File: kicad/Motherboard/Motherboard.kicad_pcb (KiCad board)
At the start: 2 copper layers, 56 parts, among them J1 USB_C_Receptacle_USB2.0, J2 Conn_01x16_Pin, J3 Conn_01x16_Pin, J4 Conn_01x16_Pin, J5 Conn_01x02_Pin, J6 Conn_01x04_Pin, J7 Conn_01x04_Pin, J8 Conn_01x16_Pin, Q1 DMN3404L, SW1 Reset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

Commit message: This commit actually has the changes
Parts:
- moved C3 46.2 mm to (179.4, 127.0)
- moved C13 45.7 mm to (162.2, 132.8)
- moved C15 45.7 mm to (222.3, 91.2)
- moved C2 45.7 mm to (222.3, 88.7)
- moved C8 45.7 mm to (137.3, 140.9)
- moved C9 45.7 mm to (162.2, 121.4)
- moved D1 45.7 mm to (145.3, 160.3)
- moved J5 45.7 mm to (150.4, 146.8)
- moved L1 45.7 mm to (156.9, 150.9)
- moved U9 45.7 mm to (135.4, 177.2)
- moved C10 45.7 mm to (162.2, 125.5)
- moved C11 45.7 mm to (162.2, 128.9)
- moved C16 45.7 mm to (193.8, 96.3)
- moved C17 45.7 mm to (193.8, 98.1)
- moved C19 45.7 mm to (222.3, 93.7)
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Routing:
- net bit3: track 0.00 -> 118.3 mm, vias 0 -> 8
- net EN2: track 0.00 -> 95.4 mm, vias 0 -> 2
- net COM2: track 0.00 -> 82.3 mm, vias 0 -> 2
- net +5V: track 0.00 -> 79.7 mm
- net bit0: track 0.00 -> 79.0 mm, vias 0 -> 4
- net bit2: track 0.00 -> 77.9 mm, vias 0 -> 4
- net EN3: track 0.00 -> 69.6 mm, vias 0 -> 2
- net COM3: track 0.00 -> 55.8 mm, vias 0 -> 2
- net EN1: track 0.00 -> 51.2 mm, vias 0 -> 2
- net COM1: track 0.00 -> 41.4 mm
- net EN0: track 0.00 -> 35.6 mm, vias 0 -> 2
- net Net-(J3-Pin_8): track 0.00 -> 23.6 mm
- net Net-(J3-Pin_9): track 0.00 -> 23.5 mm
- net Net-(J8-Pin_8): track 0.00 -> 23.3 mm
- net Net-(J4-Pin_8): track 0.00 -> 23.3 mm
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
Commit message: Didnt save yet
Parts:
- moved U7 50.8 mm to (151.0, 80.9), turned to 90 degrees
- moved J2 49.4 mm to (94.1, 68.4)
- moved U5 49.4 mm to (109.3, 136.8)
- moved U6 49.4 mm to (109.3, 110.4)
- moved SW1 49.4 mm to (119.0, 49.9)
- moved U1 49.4 mm to (143.1, 50.4)
- moved U3 49.4 mm to (109.3, 59.1)
- moved U4 49.4 mm to (109.3, 85.5)
- moved J3 49.4 mm to (94.0, 146.8)
- moved J4 49.4 mm to (94.0, 119.9)
- moved J8 49.4 mm to (94.0, 95.0)
- moved SW2 49.4 mm to (146.6, 72.1)
- moved U8 43.1 mm to (134.2, 80.4), turned to 0 degrees
- moved C12 26.3 mm to (184.0, 89.5)
- moved C13 26.3 mm to (160.8, 106.6)
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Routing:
- net bit2: track 77.9 -> 114.0 mm, vias 4 -> 8
- net GND: track 16.3 -> 0.20 mm

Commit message: idk what the fuck this is
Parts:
- moved J4 101.5 mm to (188.1, 82.0), turned to 0 degrees
- moved C2 97.4 mm to (142.1, 119.8), turned to -90 degrees
- moved J8 94.5 mm to (188.1, 103.5), turned to 0 degrees
- moved C15 94.0 mm to (142.1, 116.4), turned to 90 degrees
- moved U4 71.6 mm to (177.1, 108.5), turned to 90 degrees
- moved SW1 71.3 mm to (161.0, 107.5), turned to 180 degrees
- moved U6 69.2 mm to (177.0, 96.0), turned to 90 degrees
- moved C17 65.9 mm to (143.5, 116.0), turned to 90 degrees
- moved C19 64.5 mm to (179.0, 116.5), turned to -90 degrees
- moved C24 61.5 mm to (163.0, 112.5), turned to 0 degrees
- moved C22 57.5 mm to (163.0, 114.5), turned to 0 degrees
- moved C23 56.5 mm to (163.0, 110.5), turned to 0 degrees
- moved J1 56.3 mm to (155.5, 107.5), turned to 180 degrees
- moved C21 52.5 mm to (167.0, 112.5)
- moved J2 51.3 mm to (133.5, 101.2)
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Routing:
- net GND: track 0.20 -> 283.0 mm, vias 0 -> 11
- net +3.3V: track 0.00 -> 119.4 mm, vias 0 -> 6
- net UART_1: track 0.00 -> 118.5 mm, vias 0 -> 6
- net bit1: track 0.00 -> 106.5 mm, vias 0 -> 7
- net VS_1: track 0.00 -> 99.4 mm, vias 0 -> 7
- net COM2: track 82.3 -> 6.18 mm, vias 2 -> 0
- net VCP_1: track 0.00 -> 71.9 mm, vias 0 -> 4
- net EN2: track 95.4 -> 29.0 mm
- net ENN_2: track 0.00 -> 51.4 mm, vias 0 -> 4
- net MAGCT: track 0.00 -> 46.9 mm, vias 0 -> 4
- net Net-(U1-EN): track 18.5 -> 60.5 mm, vias 0 -> 5
- net COM3: track 55.8 -> 13.9 mm
- net +5V: track 79.7 -> 119.3 mm, vias 0 -> 4
- net Net-(D2-A): track 0.00 -> 36.3 mm
- net DIR_2: track 0.00 -> 36.1 mm, vias 0 -> 2
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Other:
- board outline added: 77 x 63 mm
- board text removed: "${REFERENCE}"

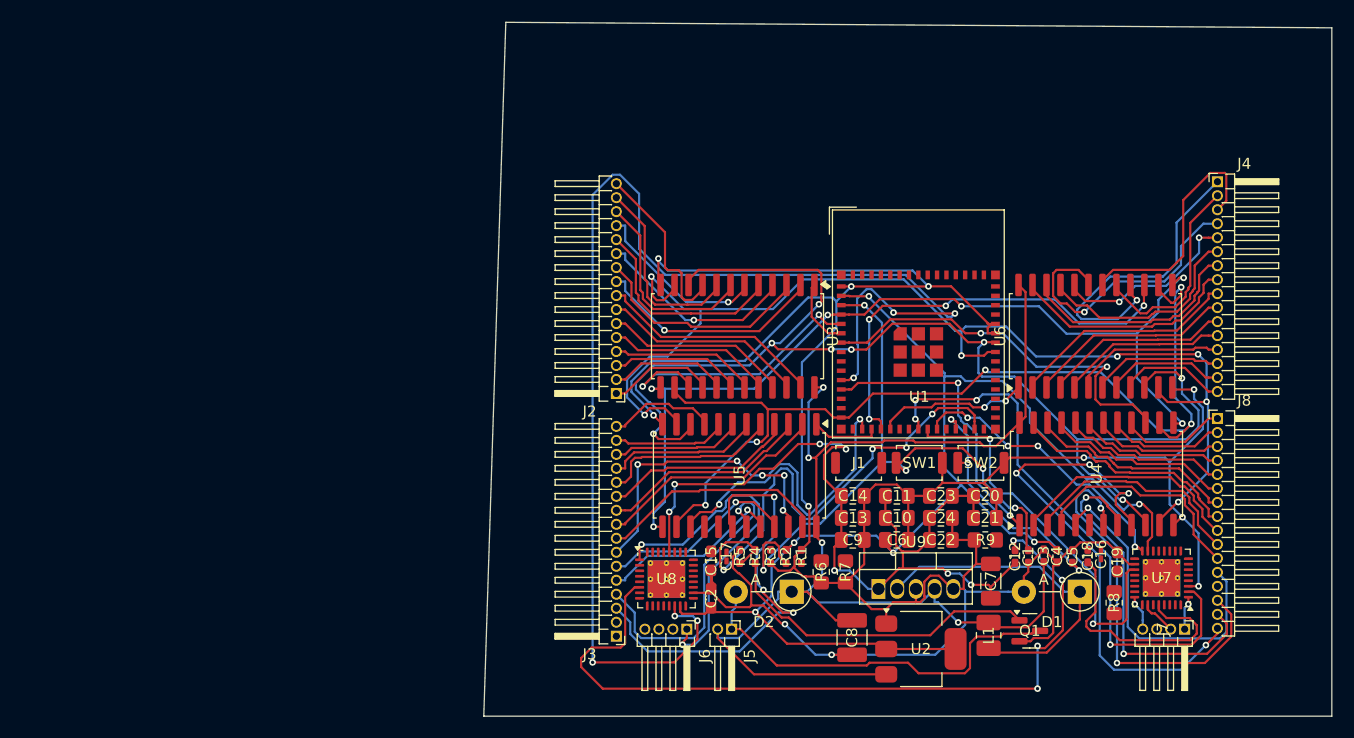
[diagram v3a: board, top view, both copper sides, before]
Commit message: updated layout
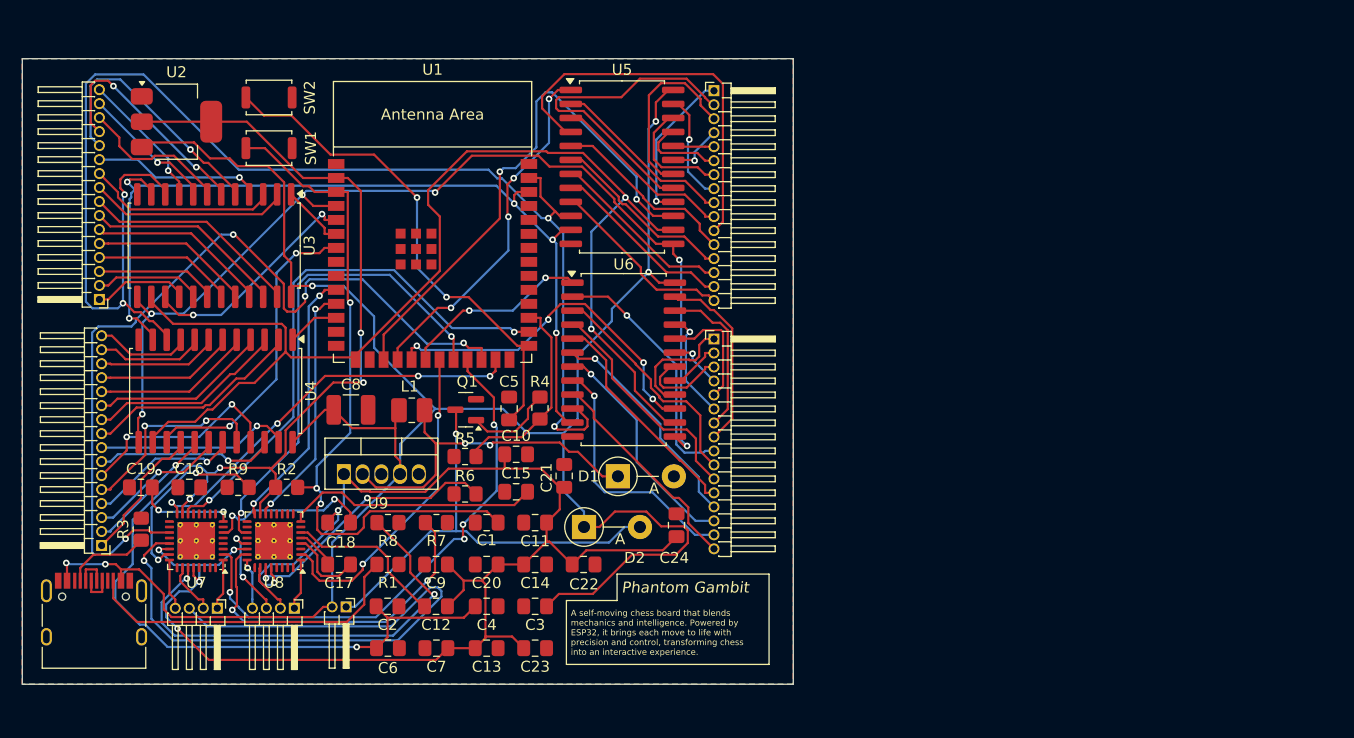
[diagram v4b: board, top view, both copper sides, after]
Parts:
- C1, C12, C18, C3, C4, C5: footprint Capacitor_SMD:C_0402_1005Metric_Pad0.74x0.62mm_HandSolder -> Capacitor_SMD:C_0805_2012Metric_Pad1.18x1.45mm_HandSolder
- C15, C19, C2: footprint Capacitor_SMD:C_0603_1608Metric_Pad1.08x0.95mm_HandSolder -> Capacitor_SMD:C_0805_2012Metric_Pad1.18x1.45mm_HandSolder
- C16, C17: footprint Capacitor_SMD:C_0201_0603Metric_Pad0.64x0.40mm_HandSolder -> Capacitor_SMD:C_0805_2012Metric_Pad1.18x1.45mm_HandSolder
- C7: footprint Capacitor_SMD:C_1206_3216Metric_Pad1.33x1.80mm_HandSolder -> Capacitor_SMD:C_0805_2012Metric_Pad1.18x1.45mm_HandSolder
- J1: footprint Button_Switch_SMD:SW_Push_SPST_NO_Alps_SKRK -> Connector_USB:USB_C_Receptacle_HRO_TYPE-C-31-M-12
- R1, R2, R3, R4, R5: footprint Resistor_SMD:R_0402_1005Metric_Pad0.72x0.64mm_HandSolder -> Resistor_SMD:R_0805_2012Metric_Pad1.20x1.40mm_HandSolder
- U1: footprint RF_Module:ESP32-S2-MINI-1 -> Espressif:ESP32-S2-SOLO
- moved J8 102.0 mm to (86.8, 115.0), turned to 180 degrees
- moved C19 88.9 mm to (90.4, 109.7), turned to 0 degrees
- moved J7 87.9 mm to (97.3, 120.7)
- moved U7 87.7 mm to (95.4, 114.6)
- moved C16 83.0 mm to (94.8, 109.7), turned to 0 degrees
- moved U2 82.8 mm to (93.6, 76.5)
- moved U4 80.3 mm to (97.2, 101.0), turned to -90 degrees
- moved SW2 72.7 mm to (102.0, 74.3)
- moved J1 71.0 mm to (86.1, 122.2), turned to 0 degrees
- moved C18 68.0 mm to (108.4, 112.9), turned to 0 degrees
- moved R9 68.0 mm to (99.2, 109.7)
- moved R8 66.3 mm to (112.8, 112.9), turned to 180 degrees
- moved SW1 65.6 mm to (102.0, 78.9)
- moved R3 57.2 mm to (90.4, 113.5), turned to 90 degrees
- moved L1 56.2 mm to (115.0, 102.7), turned to 180 degrees
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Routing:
- net GND: track 283.0 -> 0.00 mm, vias 11 -> 0
- net UART_1: track 118.5 -> 22.6 mm, vias 6 -> 2
- net +5V: track 119.3 -> 201.1 mm, vias 4 -> 5
- net Motor2_2: track 0.00 -> 63.3 mm, vias 0 -> 1
- net VCP_1: track 71.9 -> 14.7 mm, vias 4 -> 0
- net UART_2: track 0.00 -> 49.9 mm, vias 0 -> 2
- net DIR_1: track 0.00 -> 44.1 mm, vias 0 -> 2
- net Net-(U7-BRB): track 0.00 -> 41.7 mm, vias 0 -> 2
- net DIR_2: track 36.1 -> 77.3 mm, vias 2 -> 4
- net Net-(J8-Pin_16): track 48.9 -> 8.71 mm, vias 4 -> 0
- net VS_1: track 99.4 -> 134.2 mm, vias 7 -> 6
- net Net-(U8-BRA): track 0.00 -> 31.6 mm, vias 0 -> 2
- net Net-(J3-Pin_2): track 0.00 -> 30.5 mm
- net Net-(J1-CC2): track 0.00 -> 30.0 mm
- net ENN_1: track 0.00 -> 29.7 mm, vias 0 -> 2
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- added copper zone on B.Cu, net GND
- added copper zone on F.Cu, net GND
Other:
- board size 77 x 63 mm -> 70 x 56.8 mm
- board text added: "A self-moving chess board that blends mechanics and intelligence. Powered by ESP32, it brings each move to life with precision and control, transforming chess into an interactive experience."
- board text added: "Phantom Gambit"

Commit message: updated schematic
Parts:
- moved R3 84.6 mm to (172.2, 91.9), turned to 0 degrees
- moved J1 77.2 mm to (163.2, 118.0)
- moved R9 73.0 mm to (172.2, 109.6)
- moved R2 71.7 mm to (172.2, 89.0)
- moved R1 66.9 mm to (172.2, 86.0), turned to 0 degrees
- moved U2 66.0 mm to (142.9, 120.4)
- moved J8 62.8 mm to (142.6, 86.2), turned to 0 degrees
- moved SW2 62.6 mm to (134.0, 128.1)
- moved R8 59.8 mm to (172.2, 106.7), turned to 0 degrees
- moved L1 57.8 mm to (171.7, 114.1), turned to 0 degrees
- moved Q1 56.2 mm to (171.3, 125.1), turned to 0 degrees
- moved R7 55.8 mm to (172.2, 103.7), turned to 0 degrees
- moved SW1 55.0 mm to (134.0, 123.7), turned to 0 degrees
- moved U9 54.0 mm to (159.7, 126.6)
- moved J7 53.5 mm to (150.8, 121.1), turned to 0 degrees
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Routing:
- net +5V: track 201.1 -> 0.00 mm, vias 5 -> 0
- net VS_1: track 134.2 -> 0.00 mm, vias 6 -> 0
- net bit0: track 126.2 -> 0.00 mm, vias 4 -> 0
- net +3.3V: track 124.0 -> 0.00 mm, vias 5 -> 0
- net bit2: track 109.1 -> 0.00 mm, vias 2 -> 0
- net bit3: track 95.1 -> 0.00 mm, vias 6 -> 0
- net bit1: track 81.1 -> 0.00 mm, vias 5 -> 0
- net DIR_2: track 77.3 -> 0.00 mm, vias 4 -> 0
- net Net-(U1-EN): track 63.4 -> 0.00 mm, vias 3 -> 0
- net Motor2_2: track 63.3 -> 0.00 mm, vias 1 -> 0
- net UART_2: track 49.9 -> 0.00 mm, vias 2 -> 0
- net EN2: track 48.4 -> 0.00 mm, vias 2 -> 0
- net ENN_2: track 48.3 -> 0.00 mm, vias 4 -> 0
- net Net-(U1-GPIO0): track 46.0 -> 0.00 mm, vias 2 -> 0
- net DIR_1: track 44.1 -> 0.00 mm, vias 2 -> 0
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- removed copper zone on B.Cu, net GND
- removed copper zone on F.Cu, net GND
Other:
- board outline removed
- board text removed: "A self-moving chess board that blends mechanics and intelligence. Powered by ESP32, it brings each move to life with precision and control, transforming chess into an interactive experience."
- board text removed: "Phantom Gambit"

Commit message: added stuff
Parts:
- added J9: Conn_01x02_Pin, Connector_PinHeader_1.27mm:PinHeader_1x02_P1.27mm_Vertical, F.Cu at (129.6, 106.5)
- J2, J3, J4, J8: footprint Connector_PinHeader_1.27mm:PinHeader_1x16_P1.27mm_Horizontal -> Connector_PinHeader_1.27mm:PinHeader_1x16_P1.27mm_Vertical
- J5: footprint Connector_PinHeader_1.27mm:PinHeader_1x02_P1.27mm_Horizontal -> Connector_PinHeader_1.27mm:PinHeader_1x02_P1.27mm_Vertical
- J6, J7: footprint Connector_PinHeader_1.27mm:PinHeader_1x04_P1.27mm_Horizontal -> Connector_PinHeader_1.27mm:PinHeader_1x04_P1.27mm_Vertical
- moved C8 69.2 mm to (171.5, 62.2)
- moved Q1 54.6 mm to (170.9, 70.5)
- moved L1 47.9 mm to (171.1, 66.2)
- moved J2 41.5 mm to (158.8, 78.8)
- moved C1 39.5 mm to (144.7, 78.7)
- moved C10 39.5 mm to (149.5, 78.7)
- moved C11 39.5 mm to (149.5, 81.7)
- moved C12 39.5 mm to (149.5, 84.7)
- moved C13 39.5 mm to (149.5, 87.7)
- moved C14 39.5 mm to (149.5, 90.7)
- moved C15 39.5 mm to (149.5, 93.7)
- moved C16 39.5 mm to (149.5, 96.7)
- moved C17 39.5 mm to (149.5, 99.7)
- moved C18 39.5 mm to (154.4, 78.7)
- moved C19 39.5 mm to (154.4, 81.7)
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
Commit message: bet
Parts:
- J2, J3, J4, J8: footprint Connector_PinHeader_1.27mm:PinHeader_1x16_P1.27mm_Vertical -> Connector_PinHeader_2.54mm:PinHeader_1x16_P2.54mm_Vertical
- J5, J9: footprint Connector_PinHeader_1.27mm:PinHeader_1x02_P1.27mm_Vertical -> Connector_PinHeader_2.54mm:PinHeader_1x02_P2.54mm_Vertical
- J6, J7: footprint Connector_PinHeader_1.27mm:PinHeader_1x04_P1.27mm_Vertical -> Connector_PinHeader_2.54mm:PinHeader_1x04_P2.54mm_Vertical
- moved SW1 72.7 mm to (171.2, 55.4)
- moved SW2 72.7 mm to (171.2, 59.9)
- moved Q1 49.5 mm to (149.0, 114.9)
- moved J2 40.7 mm to (118.6, 72.6)
- moved J3 40.2 mm to (123.3, 72.6)
- moved J4 39.7 mm to (127.9, 72.6)
- moved J8 39.2 mm to (132.6, 72.6)
- moved R1 33.2 mm to (172.4, 71.7)
- moved R2 33.2 mm to (172.4, 74.7)
- moved R3 33.2 mm to (172.4, 77.6)
- moved R4 33.2 mm to (172.4, 80.6)
- moved R5 33.2 mm to (172.4, 83.5)
- moved R6 33.2 mm to (172.4, 86.5)
- moved R7 33.2 mm to (172.4, 89.4)
- moved R8 33.2 mm to (172.4, 92.4)
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
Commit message: TMC in
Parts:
- moved U6 148.8 mm to (67.0, 176.8), turned to 180 degrees
- moved J4 141.5 mm to (47.0, 188.7), turned to 90 degrees
- moved U3 124.3 mm to (35.0, 149.8), turned to 90 degrees
- moved U5 121.5 mm to (111.2, 177.4), turned to 180 degrees
- moved J3 120.5 mm to (91.6, 188.8), turned to 90 degrees
- moved J2 112.2 mm to (22.6, 130.7)
- moved J8 110.6 mm to (22.8, 85.4)
- moved U4 109.6 mm to (35.5, 106.2), turned to 90 degrees
- moved J6 109.3 mm to (51.2, 69.6)
- moved J7 109.3 mm to (55.9, 69.6)
- moved Q1 109.3 mm to (44.1, 84.2)
- moved U2 109.3 mm to (63.1, 80.8)
- moved C8 109.3 mm to (66.0, 33.6)
- moved R1 109.3 mm to (67.5, 41.1)
- moved R2 109.3 mm to (67.5, 44.0)
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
